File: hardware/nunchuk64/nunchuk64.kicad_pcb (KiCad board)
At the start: 2 copper layers, 50 x 41.6 mm, 28 parts, among them J1 DB9_Female, J2 DB9_Female, J3 Conn_02x03_Odd_Even, P1 CONN_WII, P2 CONN_WII, Q1 BSS138, Q2 BSS138, Q3 BSS138, Q4 BSS138, SW1 SW_Push, U1 AMS1117-3V3, U2 ATMEGA328P-AU

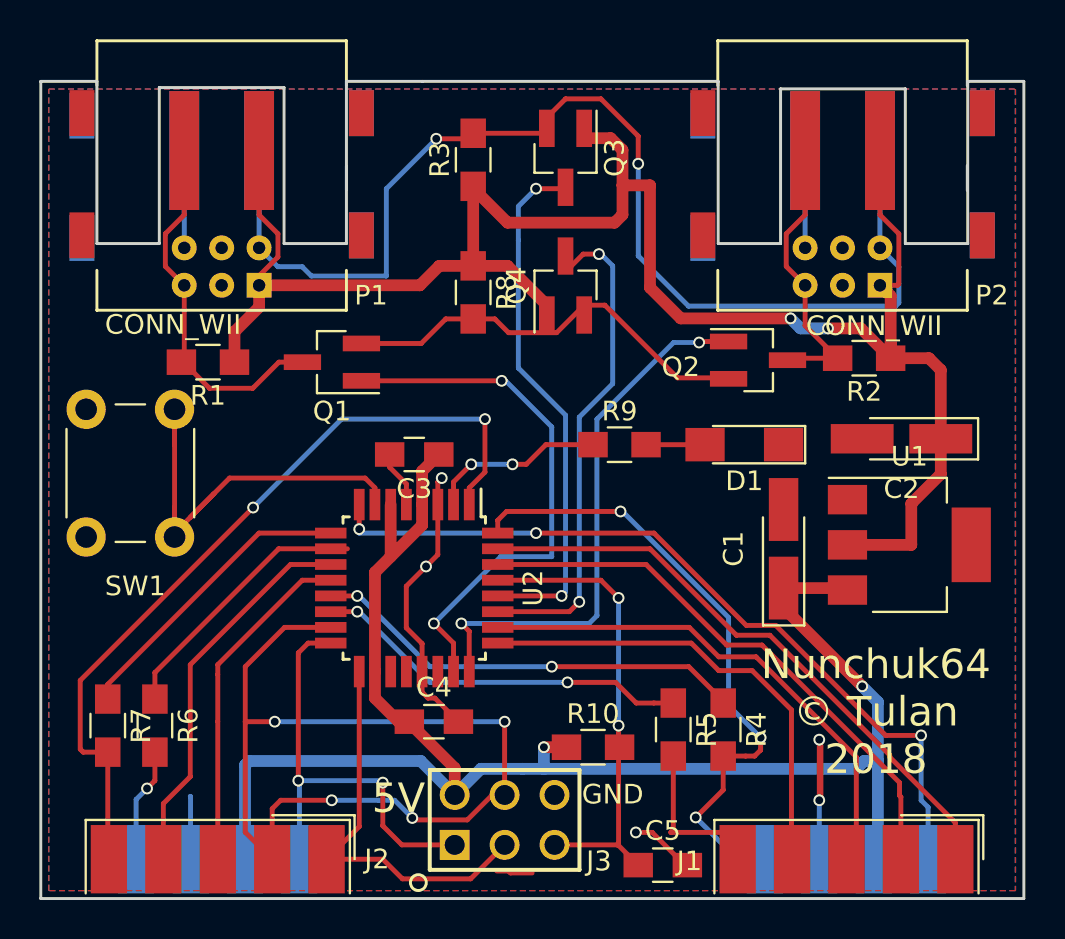
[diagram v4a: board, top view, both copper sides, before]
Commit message: rounded corners. wii_conn_edge replaces old conn
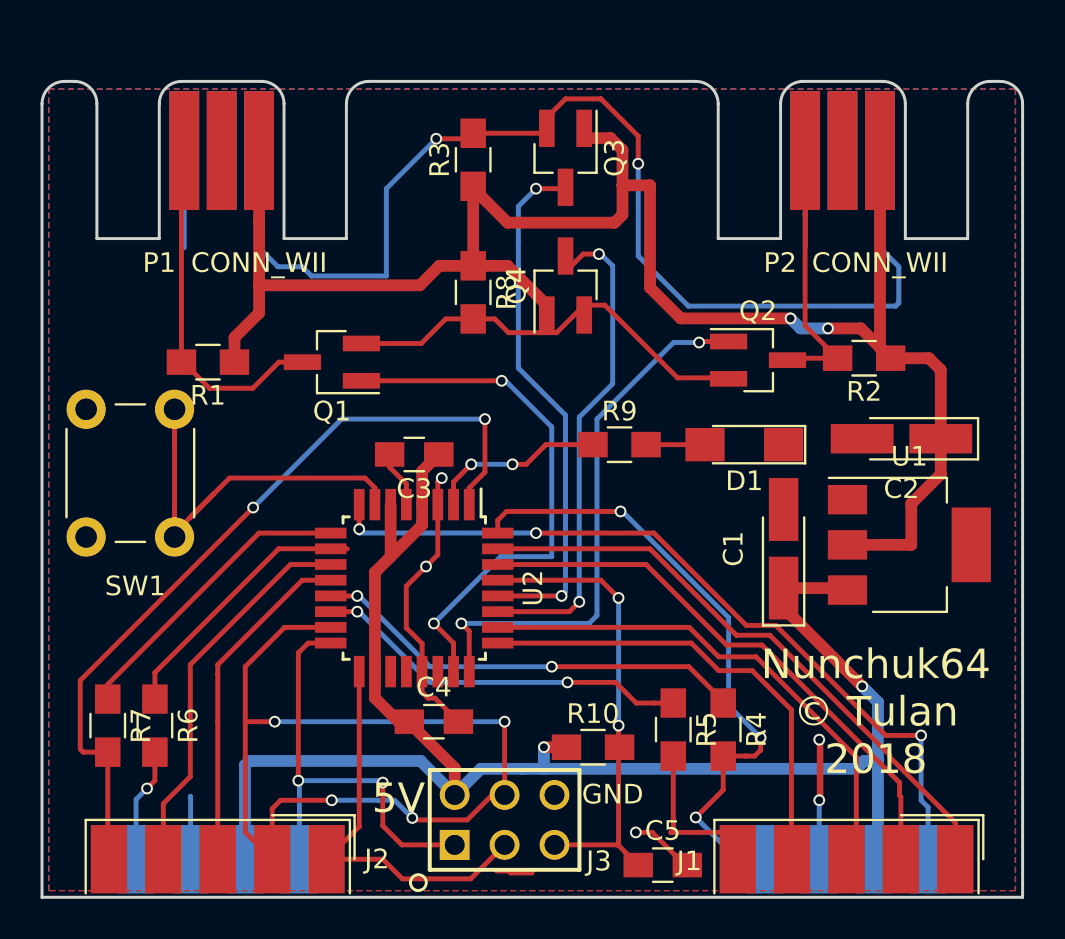
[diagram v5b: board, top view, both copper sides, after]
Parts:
- P1, P2: footprint Connectors_WII:CONN_WII -> Connectors_WII:CONN_WII_EDGECON
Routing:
- net +3V3: track 97.5 -> 92.0 mm
- net /SDA1: track 19.4 -> 18.6 mm
- net /SDA2: track 15.1 -> 14.5 mm
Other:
- board size 50 x 41.6 mm -> 49.9 x 41.5 mm
